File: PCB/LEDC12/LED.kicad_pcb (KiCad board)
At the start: 2 copper layers, 70 x 70 mm, 38 parts, among them J1 Reset, J2 Wago, J3 USB-C-Socket-H, J4 TC2030-USB-NL-DS, SW1 Button, U1 ESP32-S3-MINI-1, U2 IRMHF384, U3 ICS43434_MEMS_Mic, U4 TPS562243

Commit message: Margins tidy
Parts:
- R8: value 100k -> 150k 1%
- moved C12 0.20 mm to (110.0, 100.4)
- moved R8 0.15 mm to (110.5, 100.4), turned to -90 degrees
- moved R9 0.10 mm to (111.1, 100.4)
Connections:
- R8 pad 1: DC -> EN
- R8 pad 2: EN -> DC
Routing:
- net SW: track 9.43 -> 11.0 mm

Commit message: Re render
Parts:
- moved J4 0.10 mm to (109.5, 104.9)
- moved U2 0.07 mm to (109.7, 105.2)
- moved C10 0.05 mm to (110.3, 101.8)
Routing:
- net GND: track 61.2 -> 55.3 mm
- net +3V3: track 73.8 -> 77.7 mm
- net SCK: track 24.3 -> 25.3 mm
- net D-: track 27.6 -> 27.1 mm

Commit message: Remaker
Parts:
- added FID1: Fiducial, Fiducial:Fiducial_1mm_Mask2mm, F.Cu at (98.5, 110.0)
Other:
- board text added: "4K7 to"
- board text added: "7"
- board text removed: "+R7"
- board text removed: "⎍"

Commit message: As ordered today
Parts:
- added C2: 100nF, RevK:C_0201, F.Cu at (107.2, 98.1)
- added C3: 100nF, RevK:C_0201, F.Cu at (107.2, 98.7)
- added C4: 100nF, RevK:C_0201, F.Cu at (107.2, 99.3)
- C1: footprint RevK:C_0402 -> RevK:C_0201
- moved R2 0.93 mm to (90.3, 101.1)
- moved C1 0.20 mm to (90.1, 94.4)
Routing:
- net LED: track 17.7 -> 16.0 mm
- net GND: track 55.3 -> 54.6 mm

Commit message: Slight change
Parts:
- moved R2 0.98 mm to (89.9, 102.0)
- moved R1 0.73 mm to (106.9, 94.1)
- moved C6 0.36 mm to (106.9, 93.1)
- moved C5 0.30 mm to (89.1, 106.9)
- moved C7 0.30 mm to (89.1, 93.1)
- moved C15 0.20 mm to (107.6, 101.2)
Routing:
- net LED: track 16.0 -> 17.7 mm
- net +3V3: track 77.7 -> 76.6 mm
- net GND: vias 34 -> 35

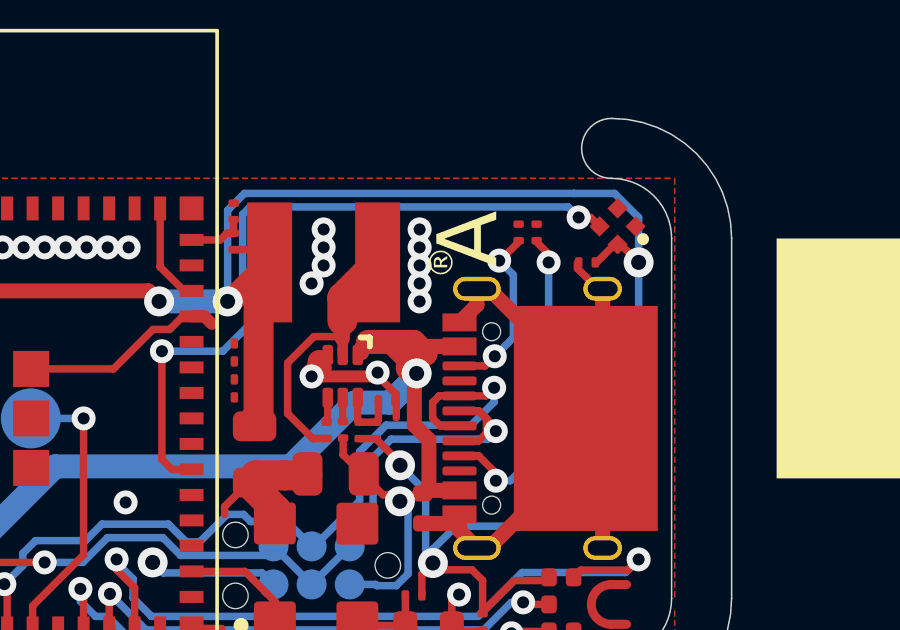
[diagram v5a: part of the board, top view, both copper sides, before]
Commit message: New LEDs
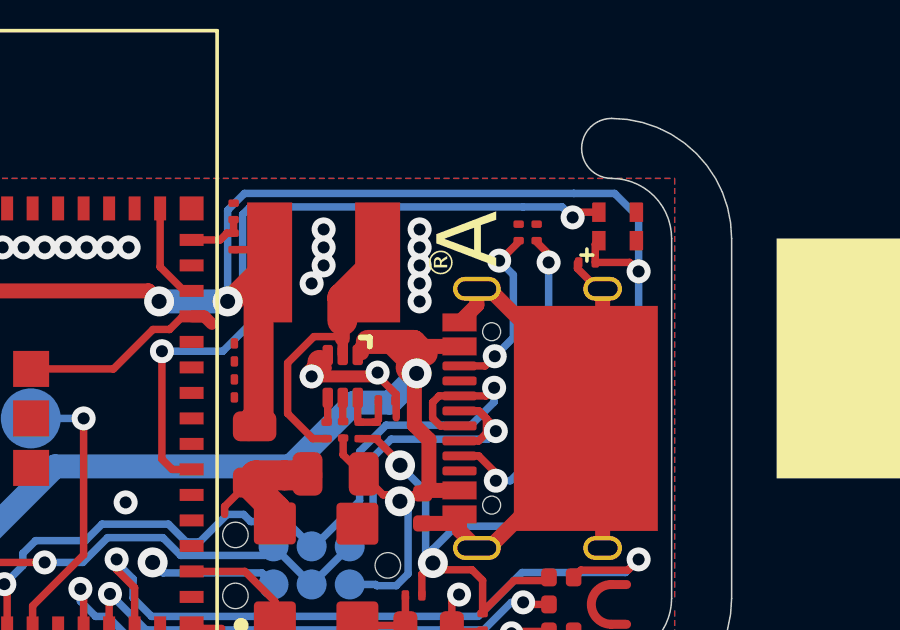
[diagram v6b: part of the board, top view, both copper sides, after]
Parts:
- D1: footprint RevK:SMD1010 -> RevK:SMD1615
- turned D1 to 180 degrees
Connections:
- D1 pad 1: unconnected-(D1-O-Pad1) -> GND
- D1 pad 2: +3V3 -> BLINK
- D1 pad 3: GND -> +3V3
- D1 pad 4: BLINK -> unconnected-(D1-O-Pad4)
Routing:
- net +3V3: track 76.6 -> 77.3 mm

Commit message: Library update
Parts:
- U1: value ESP32-S3-MINI-1 -> ESP32-S3-MINI-1-N4R2
